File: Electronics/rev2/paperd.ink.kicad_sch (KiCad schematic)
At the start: 85 parts, among them J1 USB_B_Micro, J4 EXT_CONN, Q1 DMP2035, Q2 T2N7002BK, Q3 DMP2035, Q4 DMP2035, Q5 DMP2035, Q6 UMH3N, Q7 UMH3N, Q8 T2N7002BK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

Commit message: Cleanup
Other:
- note removed: "+ Check e-paper display inductor requirement + Battery charger resistor value + Battery Sense Resistors + JST PH 2 pin for battery connector ? Reverse Polarity on the input - check in spice what would happen for existing circuit + ESD Protection + Add Auto-program circuit + Check if GPIO2 is required for the Auto-Program circuit + Confirm Buzzer circuit with respect to Piezo/Magnetic + Check Deco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"
- note removed: "- Add provison in next rev to eliminate GPIO expander"
- note removed: "NOTES:"
- note removed: "References"
- note removed: "SD Card: https://www.alliedelec.com/m/d/04db416b291011446889dbd6129e2644.pdf LED: https://hackaday.com/2017/01/20/cheating-at-5v-ws2812-control-to-use-a-3-3v-data-line/ JTAG: http://www.keil.com/support/man/docs/ulink2/ulink2_hw_connectors.htm"
- note removed: "TO-DO"
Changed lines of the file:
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@@
     (effects (font (size 2.54 2.54)) (justify left bottom))
-  )
-  (text "NOTES:" (at 303.53 66.04 0)
-    (effects (font (size 2.54 2.54) (thickness 0.508) bold) (justify left bottom))
-  )
-  (text "- Add provison in next rev to eliminate GPIO expander"
-    (at 303.53 71.12 0)
-    (effects (font (size 1.27 1.27)) (justify left bottom))
-  )
-  (text "+ Check e-paper display inductor requirement\n+ Battery charger resistor value\n+ Battery Sense Resistors\n+ JST PH 2 pin for battery connector\n? Reverse Polarity on the input - check in spice what would happen for existing circuit\n+ ESD Protection\n+ Add Auto-program circuit\n+ Check if GPIO2 is required for the Auto-Program circuit\n+ Confirm Buzzer circuit with respect to Piezo/Magnetic\n+ Check Decoupling capacitors\n- Check LED Resistors\n\n\n\n\n\n\n\n\n\n\n\n\n\n\n\n\n\n\n\n\n\n\n\n\n\n\n"
-    (at 303.53 100.33 0)
-    (effects (font (size 1.27 1.27)) (justify left bottom))
-  )
-  (text "TO-DO" (at 304.8 20.32 0)
-    (effects (font (size 2.54 2.54) (thickness 0.508) bold) (justify left bottom))
-  )
-  (text "References" (at 304.8 111.76 0)
-    (effects (font (size 2.54 2.54) (thickness 0.508) bold) (justify left bottom))
-  )
-  (text "SD Card: https://www.alliedelec.com/m/d/04db416b291011446889dbd6129e2644.pdf\nLED: https://hackaday.com/2017/01/20/cheating-at-5v-ws2812-control-to-use-a-3-3v-data-line/\nJTAG: http://www.keil.com/support/man/docs/ulink2/ulink2_hw_connectors.htm\n"
-    (at 304.8 119.38 0)
-    (effects (font (size 1.27 1.27)) (justify left bottom))
   )
   (text "-" (at 306.07 148.59 0)

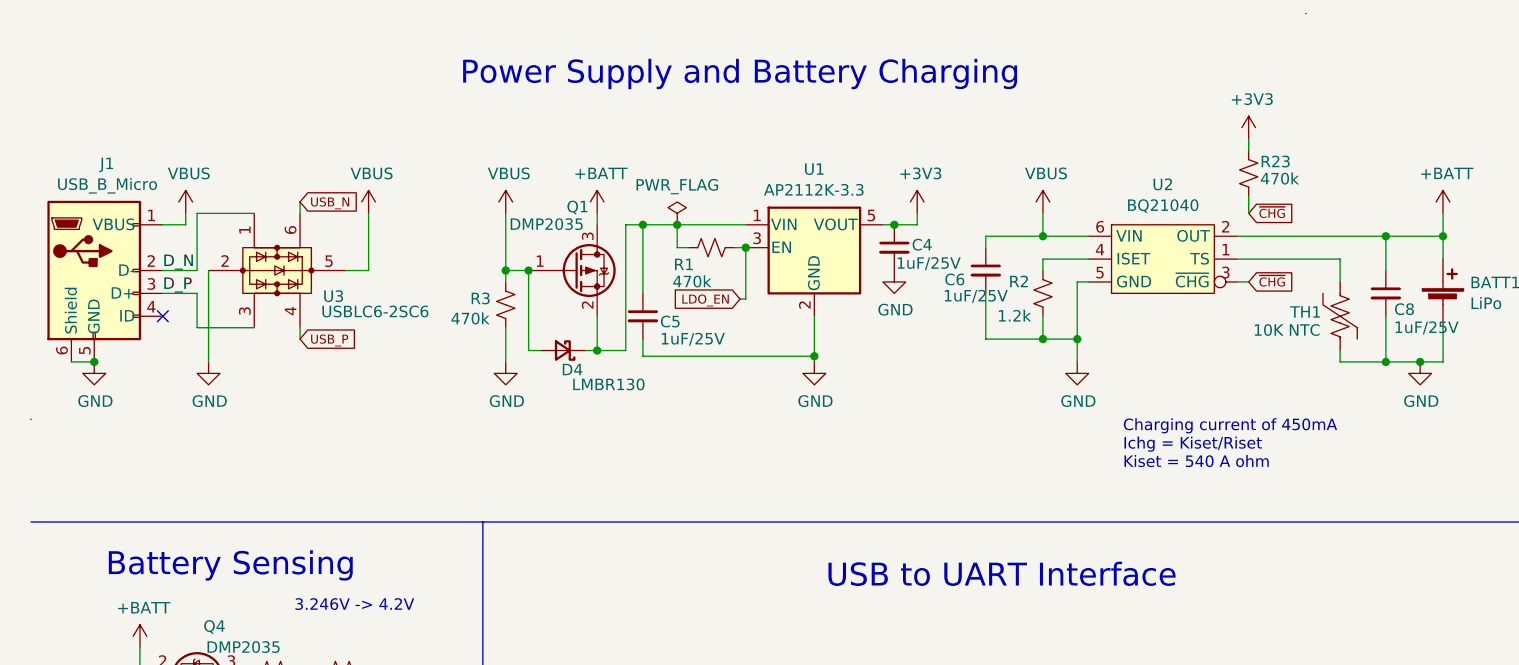
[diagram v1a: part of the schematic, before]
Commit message: Made few changes
1) Added fuse
2) Changed battery connector to smaller one since this was too tall
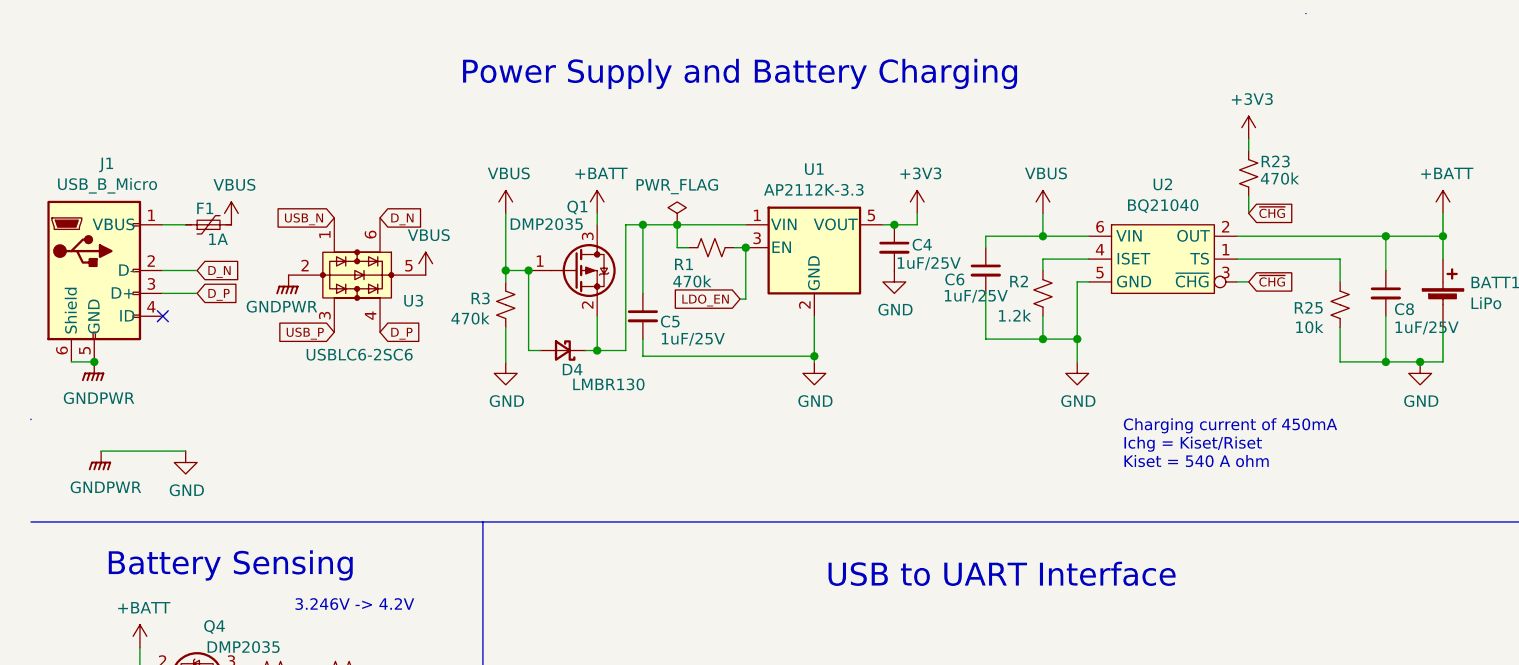
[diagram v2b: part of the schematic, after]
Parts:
- removed TH1: 10K NTC, Resistor_SMD:R_0402_1005Metric, symbol Device:Thermistor_US
- added F1: 1A, Fuse:Fuse_0805_2012Metric, symbol Device:Polyfuse_Small
- added R25: 10k, Resistor_SMD:R_0402_1005Metric, symbol Device:R_Small_US
- BATT1: footprint Connector_JST:JST_PH_B2B-PH-SM4-TB_1x02-1MP_P2.00mm_Vertical -> karo_industries:Connector_1x02_P1.25mm_Horizontal; Link https://lcsc.com/product-detail/Wire-To-Board-Wire-To-Wire-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 -> (none)
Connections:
- net D_N: now also U3.6 (IO1); no longer U3.1 (IO1)
- net D_P: now also U3.4 (IO2); no longer U3.3 (IO2)
- net GND: now also R25.2
- net USB_N: now also U3.1 (IO1); no longer U3.6 (IO1)
- net USB_P: now also U3.3 (IO2); no longer U3.4 (IO2)
- net VBUS: now also F1.2; no longer J1.1 (VBUS)
- net at U2.1 (TS): now also R25.1
- new net: F1.1, J1.1 (VBUS)
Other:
- moved on the sheet: U3
